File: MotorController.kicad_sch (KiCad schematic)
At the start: 131 parts, among them IC1 ft234xd, IC2 A3921KLPTR-T, IC3 A3921KLPTR-T, J1 SH, J10 XT30, J11 XT30, J2 USB_B_Micro, J3 XA, J4 XA, J5 3020-10-0300-00, J6 SH, J7 SH, J8 3020-10-0300-00, J9 XA, Q1 GSFQ6806, Q2 GSFQ6806, Q3 GSFQ6806, Q4 SFS9Z34, Q5 GSFQ6806, Q6 SFS9Z34, SW2 BLACK, SW3 BLACK, SW4 2MS1-T1-B4-VS2-Q-E-S, SW5 RED, U1 LXES11D, U2 STM32F303K8Tx, U3 TJA1441AT, U4 TPSM13604HNDWR, U5 LMZ12002EXT, Y1 32M

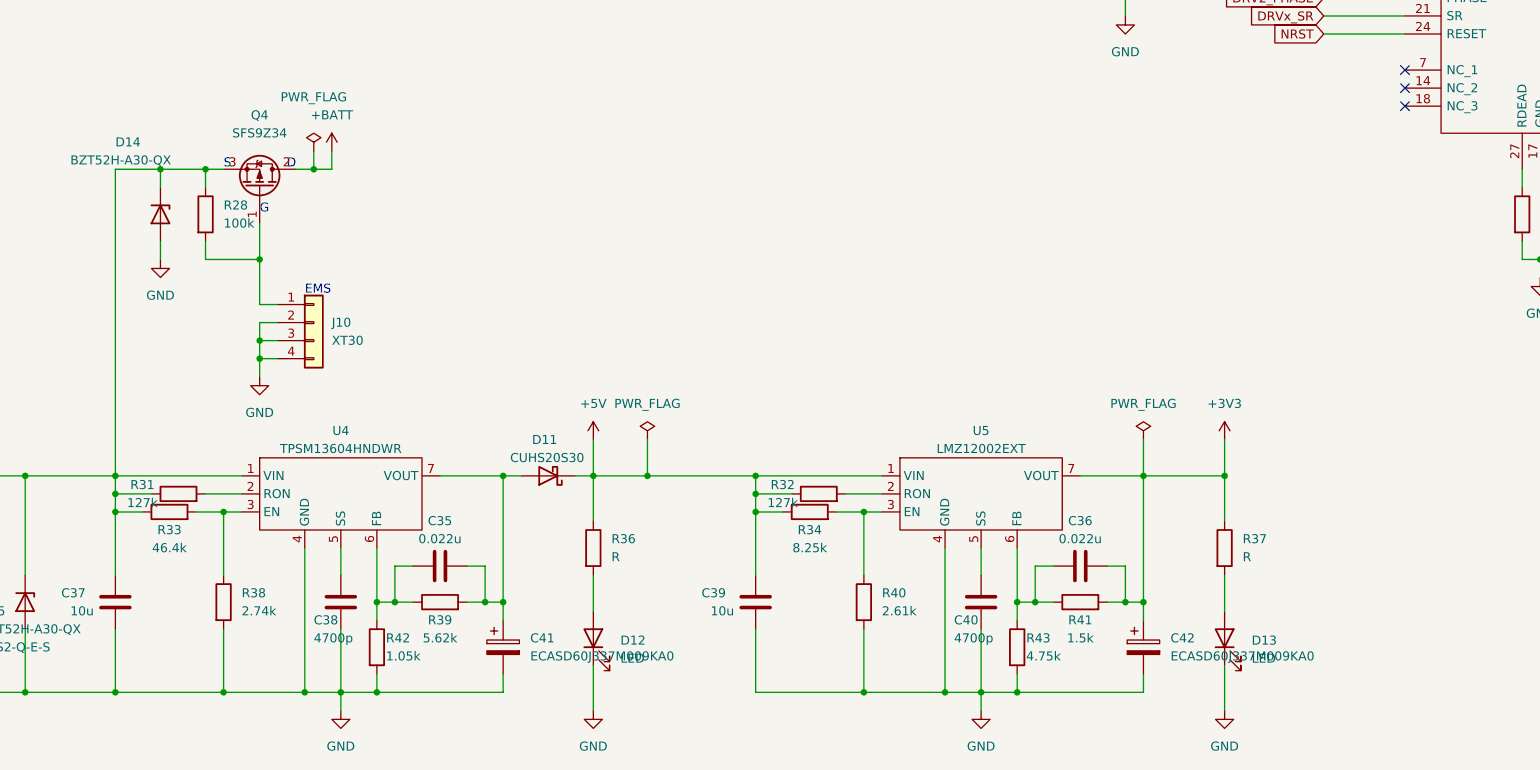
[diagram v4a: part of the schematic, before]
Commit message: 電源回路設置完了！USB の回路設置中
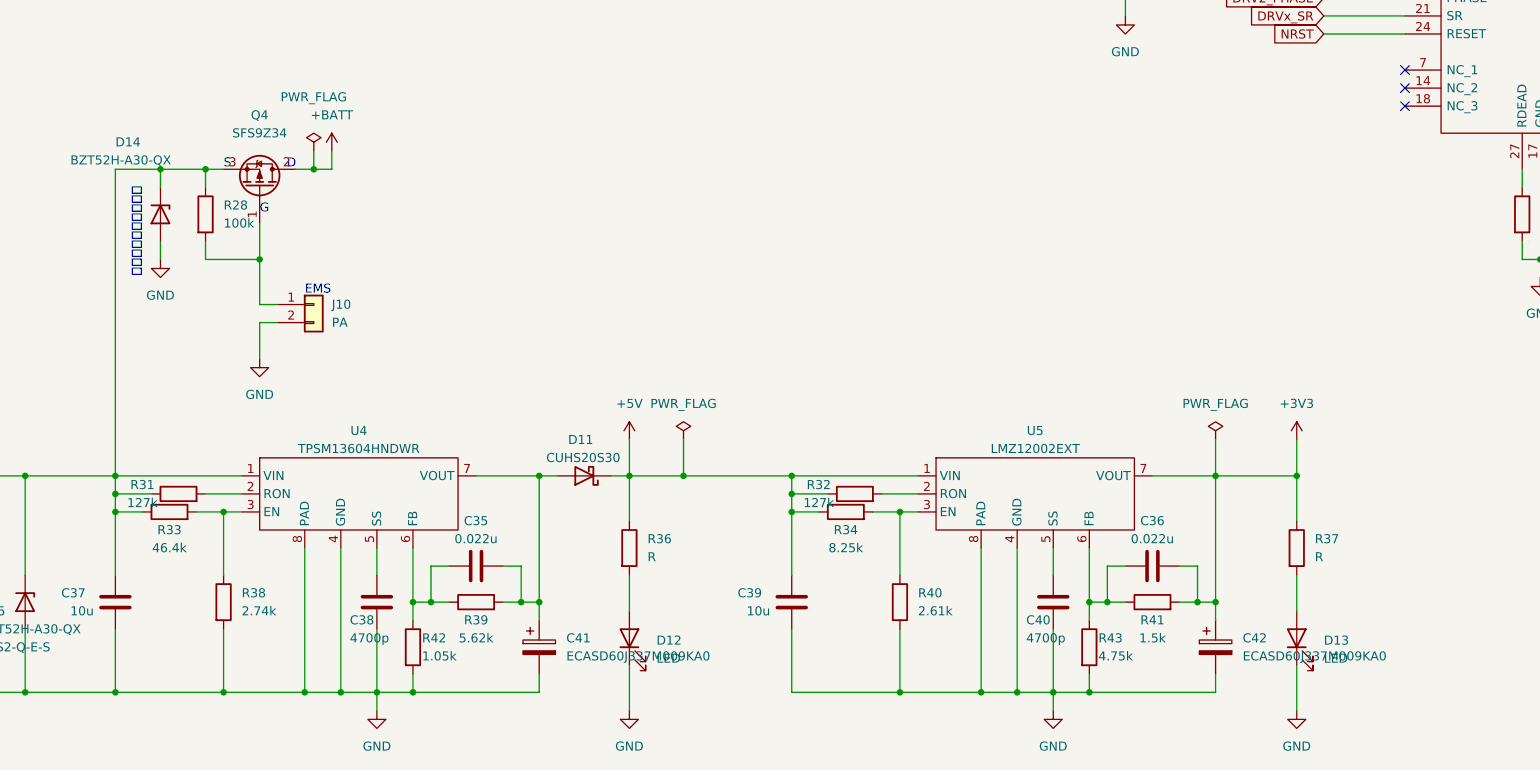
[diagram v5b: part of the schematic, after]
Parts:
- removed J10: XT30, LibraryLoader:XT30PWM, symbol Connector_Generic:Conn_01x04
- added J10: PA, LibraryLoader:PA_01x02, symbol Connector_Generic:Conn_01x02
- J5, J8: footprint Connector_IDC:IDC-Header_2x10_P2.54mm_Vertical -> Connector_IDC:IDC-Header_2x05_P2.54mm_Vertical
- Q1, Q2, Q3, Q5: footprint Package_SO:HSOP-8-1EP_3.9x4.9mm_P1.27mm_EP2.3x2.3mm -> Package_SO:SO-8_3.9x4.9mm_P1.27mm
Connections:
- net GND: now also U4.8 (PAD), U5.8 (PAD), J10.2 (Pin_2)
- net at Q4.1 (G), R28.2: now also J10.1 (Pin_1)
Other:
- note added: "ここじゃないのか疑問"
- moved on the sheet: C35, C36, C38, C39, C40, C41, C42, D11, D12, D13, R32, R34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

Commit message: Z 実装
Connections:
- net GND: no longer D14.2 (A), D15.2 (A)
- net at J10.1 (Pin_1), Q4.1 (G), R28.2: now also D14.2 (A)
- net at C37.1, D14.1 (K), Q4.3 (S)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: no longer D15.1 (K)
- net at Q6.1 (G), R35.2, SW4.3 (C): now also D15.2 (A)
- net at J11.1 (Pin_1), Q6.3 (S), R35.1: now also D15.1 (K)
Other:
- note added: "UART"
- note removed: "ここじゃないのか疑問"
- moved on the sheet: C23, C33, D15, J11, J5, J8, Q6, R17, R18, R24, R25, R35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

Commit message: CPU CAN MD DCDC の位置感決めた あとは UI
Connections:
- net DRV1_PWMH: now also IC2.22 (PWML); no longer IC2.23 (PWMH)
- net DRV1_PWML: now also IC2.23 (PWMH); no longer IC2.22 (PWML)
- net Encoder_LA: now also U2.18 (PA8); no longer U2.19 (PA9)
- net Encoder_LB: now also U2.19 (PA9); no longer U2.18 (PA8)
- net Encoder_RA: now also U2.7 (PA1); no longer U2.11 (PA5)
- net Encoder_RB: now also U2.11 (PA5); no longer U2.7 (PA1)
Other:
- note added: "← 14 mA"
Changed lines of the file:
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@@
     (effects (font (size 1.27 1.27)) (justify right bottom))
+  )
+  (text "← 14 mA" (at 279.4 33.02 90)
+    (effects (font (size 1.27 1.27)) (justify left bottom))
   )
   (text "SWD" (at 166.37 146.05 0)
@@
     )
   )
-  (global_label "Encoder_RA" (shape input) (at 129.54 86.36 0) (fields_autoplaced)
+  (global_label "Encoder_RA" (shape input) (at 129.54 76.2 0) (fields_autoplaced)
     (effects (font (size 1.27 1.27)) (justify left))
-    (property "Intersheetrefs" "${INTERSHEET_REFS}" (at 143.4108 86.36 0)
+    (property "Intersheetrefs" "${INTERSHEET_REFS}" (at 143.4108 76.2 0)
       (effects (font (size 1.27 1.27)) (justify left) hide)
     )
@@
     )
   )
-  (global_label "Encoder_RB" (shape input) (at 129.54 76.2 0) (fields_autoplaced)
+  (global_label "Encoder_RB" (shape input) (at 129.54 86.36 0) (fields_autoplaced)
     (effects (font (size 1.27 1.27)) (justify left))
-    (property "Intersheetrefs" "${INTERSHEET_REFS}" (at 143.5922 76.2 0)
+    (property "Intersheetrefs" "${INTERSHEET_REFS}" (at 143.5922 86.36 0)
       (effects (font (size 1.27 1.27)) (justify left) hide)
     )
@@
     )
   )
-  (global_label "Encoder_LA" (shape input) (at 129.54 96.52 0) (fields_autoplaced)
+  (global_label "Encoder_LA" (shape input) (at 129.54 93.98 0) (fields_autoplaced)
     (effects (font (size 1.27 1.27)) (justify left))
-    (property "Intersheetrefs" "${INTERSHEET_REFS}" (at 143.1689 96.52 0)
+    (property "Intersheetrefs" "${INTERSHEET_REFS}" (at 143.1689 93.98 0)
       (effects (font (size 1.27 1.27)) (justify left) hide)
     )
@@
     )
   )
-  (global_label "DRV1_PWML" (shape input) (at 255.27 64.77 180) (fields_autoplaced)
+  (global_label "DRV1_PWML" (shape input) (at 255.27 62.23 180) (fields_autoplaced)
     (effects (font (size 1.27 1.27)) (justify right))
-    (property "Intersheetrefs" "${INTERSHEET_REFS}" (at 241.2782 64.77 0)
+    (property "Intersheetrefs" "${INTERSHEET_REFS}" (at 241.2782 62.23 0)
       (effects (font (size 1.27 1.27)) (justify right) hide)
     )
@@
     )
   )
-  (global_label "DRV1_PWMH" (shape input) (at 255.27 62.23 180) (fields_autoplaced)
+  (global_label "DRV1_PWMH" (shape input) (at 255.27 64.77 180) (fields_autoplaced)
     (effects (font (size 1.27 1.27)) (justify right))
-    (property "Intersheetrefs" "${INTERSHEET_REFS}" (at 240.9758 62.23 0)
+    (property "Intersheetrefs" "${INTERSHEET_REFS}" (at 240.9758 64.77 0)
       (effects (font (size 1.27 1.27)) (justify right) hide)
     )
@@
     )
   )
-  (global_label "Encoder_LB" (shape input) (at 129.54 93.98 0) (fields_autoplaced)
+  (global_label "Encoder_LB" (shape input) (at 129.54 96.52 0) (fields_autoplaced)
     (effects (font (size 1.27 1.27)) (justify left))
-    (property "Intersheetrefs" "${INTERSHEET_REFS}" (at 143.3503 93.98 0)
+    (property "Intersheetrefs" "${INTERSHEET_REFS}" (at 143.3503 96.52 0)
       (effects (font (size 1.27 1.27)) (justify left) hide)
     )

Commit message: GND ベタを塗る直前までやった
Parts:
- added H1, H2: MountingHole, MountingHole:MountingHole_3.2mm_M3, symbol Mechanical:MountingHole
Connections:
- net GND: now also D14.2 (A), D15.2 (A)
- net at J10.1 (Pin_1), Q4.1 (G), R28.2: no longer D14.2 (A)
- net at Q6.1 (G), R35.2, SW4.3 (C): no longer D15.2 (A)
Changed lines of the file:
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@@
   (junction (at 129.54 261.62) (diameter 0) (color 0 0 0 0)
   )
+  (junction (at 105.41 222.25) (diameter 0) (color 0 0 0 0)
+  )
   (junction (at 219.71 100.33) (diameter 0) (color 0 0 0 0)
   )
@@
   (junction (at 91.44 200.66) (diameter 0) (color 0 0 0 0)
   )
-  (junction (at 97.79 213.36) (diameter 0) (color 0 0 0 0)
-  )
   (junction (at 354.33 102.87) (diameter 0) (color 0 0 0 0)
   )
@@
   (junction (at 179.07 60.96) (diameter 0) (color 0 0 0 0)
   )
+  (junction (at 60.96 274.32) (diameter 0) (color 0 0 0 0)
+  )
   (junction (at 111.76 60.96) (diameter 0) (color 0 0 0 0)
   )
@@
   (junction (at 49.53 194.31) (diameter 0) (color 0 0 0 0)
   )
-  (junction (at 67.31 256.54) (diameter 0) (color 0 0 0 0)
-  )
   (junction (at 251.46 243.84) (diameter 0) (color 0 0 0 0)
   )
@@
     (stroke (width 0) (type default))
   )
-  (wire (pts (xy 44.45 274.32) (xy 66.04 274.32))
+  (wire (pts (xy 44.45 274.32) (xy 60.96 274.32))
     (stroke (width 0) (type default))
   )
@@
     (stroke (width 0) (type default))
   )
-  (wire (pts (xy 60.96 254) (xy 60.96 256.54))
-    (stroke (width 0) (type default))
-  )
   (wire (pts (xy 207.01 76.2) (xy 189.23 76.2))
     (stroke (width 0) (type default))
@@
     (stroke (width 0) (type default))
   )
-  (wire (pts (xy 60.96 256.54) (xy 67.31 256.54))
-    (stroke (width 0) (type default))
-  )
   (wire (pts (xy 233.68 146.05) (xy 240.03 146.05))
     (stroke (width 0) (type default))
@@
     (stroke (width 0) (type default))
   )
-  (wire (pts (xy 91.44 213.36) (xy 97.79 213.36))
-    (stroke (width 0) (type default))
-  )
   (wire (pts (xy 113.03 88.9) (xy 129.54 88.9))
     (stroke (width 0) (type default))
@@
     (stroke (width 0) (type default))
   )
+  (wire (pts (xy 91.44 222.25) (xy 105.41 222.25))
+    (stroke (width 0) (type default))
+  )
   (wire (pts (xy 46.99 248.92) (xy 44.45 248.92))
     (stroke (width 0) (type default))
@@
     (stroke (width 0) (type default))
   )
+  (wire (pts (xy 60.96 274.32) (xy 66.04 274.32))
+    (stroke (width 0) (type default))
+  )
   (wire (pts (xy 354.33 24.13) (xy 354.33 26.67))
     (stroke (width 0) (type default))
@@
     (stroke (width 0) (type default))
   )
+  (wire (pts (xy 60.96 254) (xy 60.96 274.32))
+    (stroke (width 0) (type default))
+  )
   (wire (pts (xy 130.81 34.29) (xy 130.81 36.83))
     (stroke (width 0) (type default))
@@
     (stroke (width 0) (type default))
   )
-  (wire (pts (xy 91.44 210.82) (xy 91.44 213.36))
+  (wire (pts (xy 91.44 210.82) (xy 91.44 222.25))
     (stroke (width 0) (type default))
   )
@@
     )
   )
+  (symbol (lib_id "Mechanical:MountingHole") (at 276.86 248.92 0) (unit 1)
+    (in_bom yes) (on_board yes) (dnp no)
+    (property "Reference" "H2" (at 280.67 247.65 0)
+      (effects (font (size 1.27 1.27)))
+    )
+    (property "Value" "MountingHole" (at 285.75 250.19 0)
+      (effects (font (size 1.27 1.27)))
+    )
+    (property "Footprint" "MountingHole:MountingHole_3.2mm_M3" (at 276.86 248.92 0)
+      (effects (font (size 1.27 1.27)) hide)
+    )
+    (property "Datasheet" "~" (at 276.86 248.92 0)
+      (effects (font (size 1.27 1.27)) hide)
+    )
+    (instances
+      (project "MotorController"
+        (path "/5f98a318-5528-4c4b-bcf3-90ead89a063c"
+          (reference "H2") (unit 1)
+        )
+      )
+    )
+  )
   (symbol (lib_id "Device:R") (at 222.25 267.97 0) (unit 1)
     (in_bom yes) (on_board yes) (dnp no)
@@
         )
       )
+    )
+  )
+  (symbol (lib_id "Mechanical:MountingHole") (at 276.86 243.84 0) (unit 1)
+    (in_bom yes) (on_board yes) (dnp no) (fields_autoplaced)
+    (property "Reference" "H1" (at 279.4 243.205 0)
+      (effects (font (size 1.27 1.27)) (justify left))
+    )
+    (property "Value" "MountingHole" (at 279.4 245.745 0)
+      (effects (font (size 1.27 1.27)) (justify left))
+    )
+    (property "Footprint" "MountingHole:MountingHole_3.2mm_M3" (at 276.86 243.84 0)
+      (effects (font (size 1.27 1.27)) hide)
+    )
+    (property "Datasheet" "~" (at 276.86 243.84 0)
+      (effects (font (size 1.27 1.27)) hide)
+    )
+    (instances
+      (project "MotorController"
+        (path "/5f98a318-5528-4c4b-bcf3-90ead89a063c"
+          (reference "H1") (unit 1)
+        )
+      )
